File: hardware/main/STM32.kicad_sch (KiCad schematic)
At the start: 39 parts, among them U201 REF3430QDGKRQ1, U202 STM32L431RCTx

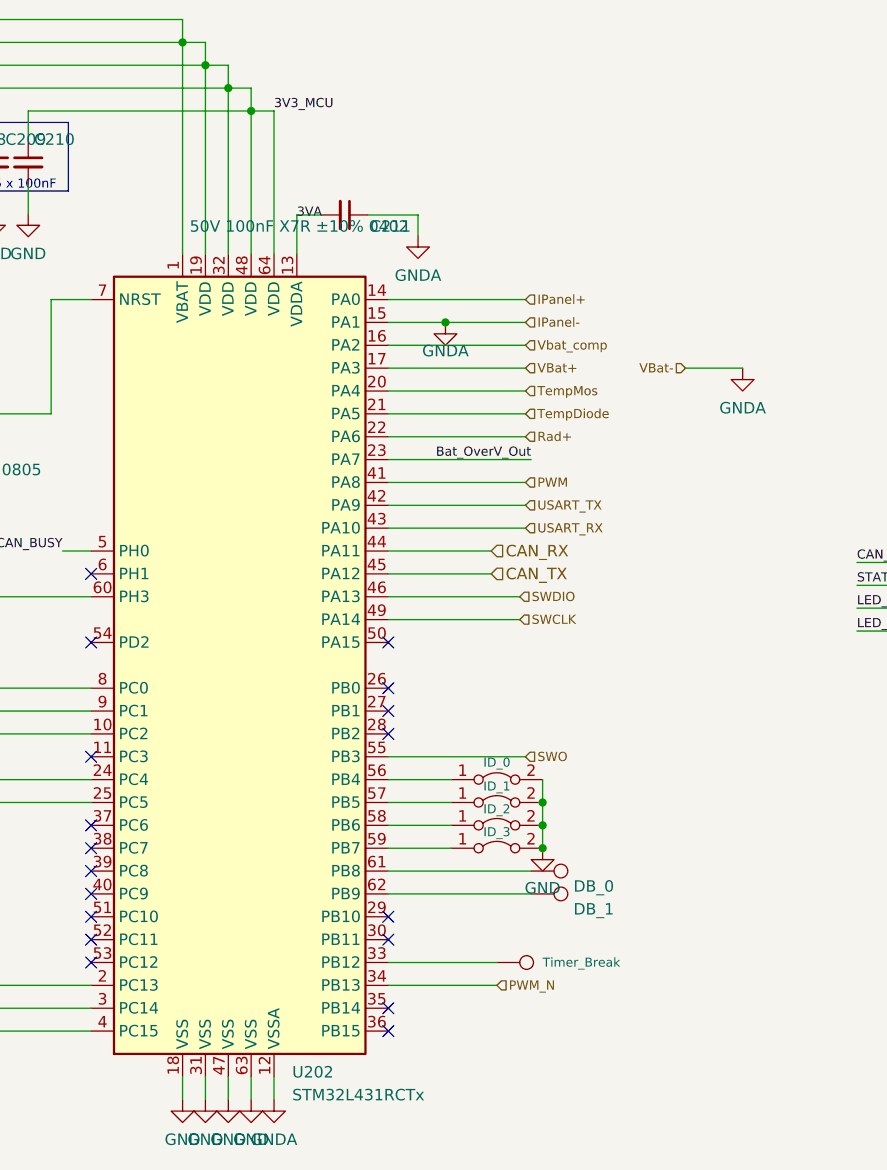
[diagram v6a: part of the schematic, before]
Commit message: Layout: Finalize first vesion of control (DRC ok) and modify vias for better via density
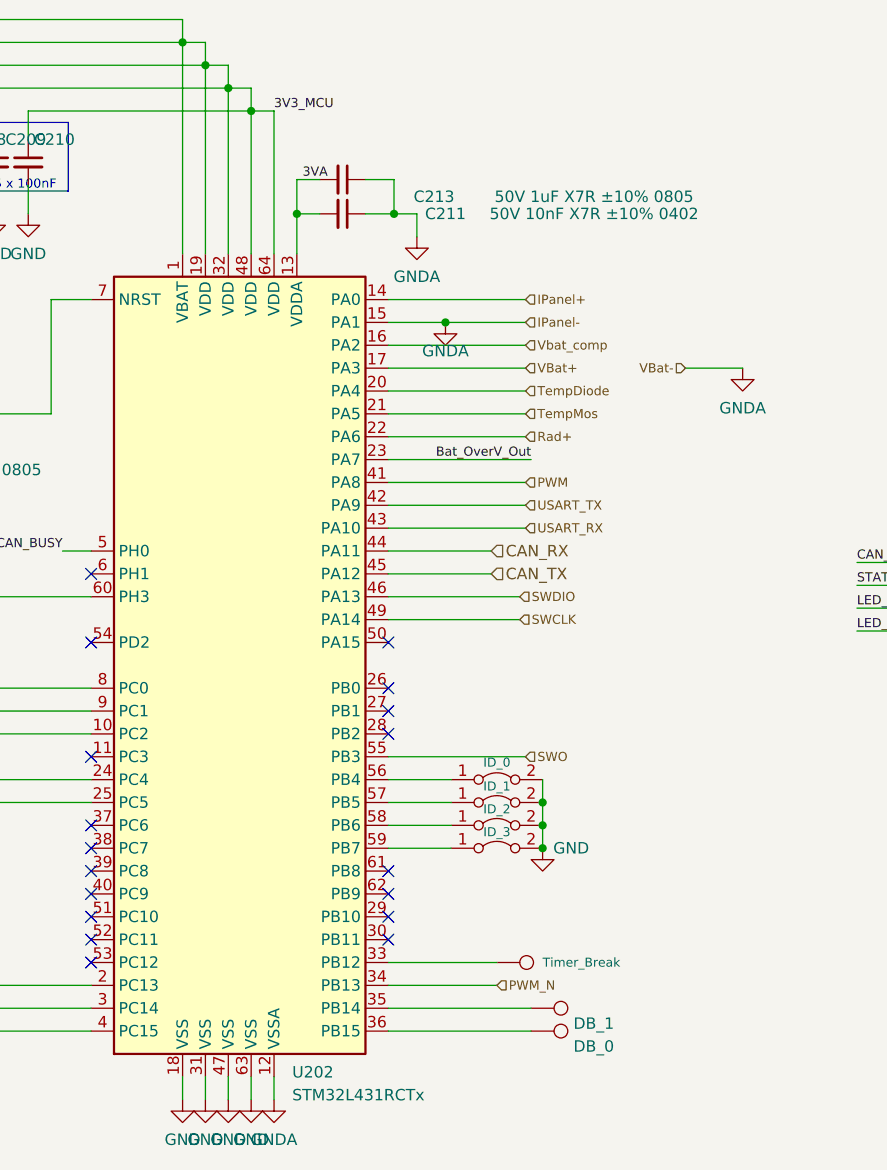
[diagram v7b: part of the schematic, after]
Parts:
- added C213: 50V 1uF X7R ±10% 0805, Capacitor_SMD:C_0805_2012Metric_Pad1.18x1.45mm_HandSolder, symbol Device:C_Small
- C211: value 50V 100nF X7R ±10% 0402 -> 50V 10nF X7R ±10% 0402
- NT201, NT202, NT203: footprint Resistor_SMD:R_0201_0603Metric -> Zenite:NetTie-2_SMD_Pad0.3mm
- TP201, TP202: footprint TestPoint:TestPoint_Pad_1.5x1.5mm -> Zenite:TestPoint_Pad_1.0x1.0mm_small
- TP203: footprint TestPoint:TestPoint_Pad_1.0x1.0mm -> Zenite:TestPoint_Pad_1.0x1.0mm_small
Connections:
- net 3VA: now also C213.2
- net GNDA: now also C213.1
- net TempDiode: now also U202.20 (PA4); no longer U202.21 (PA5)
- net TempMos: now also U202.21 (PA5); no longer U202.20 (PA4)
- net at TP201.1: now also U202.36 (PB15); no longer U202.61 (PB8)
- net at TP202.1: now also U202.35 (PB14); no longer U202.62 (PB9)
